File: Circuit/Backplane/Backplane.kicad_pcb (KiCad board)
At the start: 2 copper layers, 90.2 x 288.5 mm, 86 parts, among them CON1 Peripheral bridge, CON2 Power distributor, J1 USB_OTG, J2 power_source_mode, J3 general_power_source, J4 pneumatic, J5 pressure_sensor, J6 RS232_DVL, P1 imaging_sonar, P2 DVL, P3 computer1, P4 computer2, P5 ethernet_switch, P6 general, Q1 BC817-40, U1 LM1117-3.3, U2 TUSB4041I, U3 TLV73311PDBVT, Y1 24MHz

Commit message: re-commmit edit
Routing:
- net GND: track 74.5 -> 94.5 mm, vias 8 -> 14
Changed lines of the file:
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@@
     (thickness 1.6)
     (drawings 52)
-    (tracks 1115)
+    (tracks 1135)
     (zones 0)
     (modules 86)
@@
   )
   (setup
-    (last_trace_width 0.254)
+    (last_trace_width 0.381)
     (user_trace_width 0.381)
     (user_trace_width 0.508)
@@
     (user_trace_width 1.27)
     (trace_clearance 0.2032)
-    (zone_clearance 0.1524)
+    (zone_clearance 0.381)
     (zone_45_only no)
     (trace_min 0.2032)
@@
   (segment (start 155.966 254.332) (end 155.028 255.27) (width 0.254) (layer F.Cu) (net 2))
   (segment (start 155.966 253.432) (end 155.966 254.332) (width 0.254) (layer F.Cu) (net 2))
+  (segment (start 163.8 26.8) (end 163.8 25.969) (width 0.381) (layer F.Cu) (net 3))
+  (segment (start 163.8 25.969) (end 165.02379 24.74521) (width 0.381) (layer F.Cu) (net 3))
+  (segment (start 165.02379 24.74521) (end 165.02379 13.757744) (width 0.381) (layer F.Cu) (net 3))
+  (segment (start 165.02379 13.757744) (end 163.8632 12.597154) (width 0.381) (layer F.Cu) (net 3))
+  (segment (start 163.8632 12.597154) (end 163.8632 11.589313) (width 0.381) (layer F.Cu) (net 3))
   (segment (start 139.446 36.576) (end 140.72871 35.29329) (width 0.381) (layer F.Cu) (net 3))
   (segment (start 140.72871 35.29329) (end 155.19151 35.29329) (width 0.381) (layer F.Cu) (net 3))
   (segment (start 155.19151 35.29329) (end 163.7132 26.7716) (width 0.381) (layer F.Cu) (net 3))
   (segment (start 163.7132 26.7716) (end 163.8632 26.7716) (width 0.381) (layer F.Cu) (net 3))
-  (segment (start 164.85006 13.584014) (end 163.8632 12.597154) (width 0.381) (layer F.Cu) (net 3))
-  (segment (start 163.8632 12.597154) (end 163.8632 11.589313) (width 0.381) (layer F.Cu) (net 3))
   (segment (start 96.52 193.04) (end 86.36 203.2) (width 0.381) (layer F.Cu) (net 3))
   (segment (start 86.36 203.2) (end 86.36 251.46) (width 0.381) (layer F.Cu) (net 3))
@@
   (segment (start 139.446 36.576) (end 116.84 59.182) (width 0.381) (layer B.Cu) (net 3))
   (via (at 139.446 36.576) (size 1.10236) (drill 0.6096) (layers F.Cu B.Cu) (net 3))
-  (segment (start 164.85006 13.584014) (end 164.85006 24.91894) (width 0.381) (layer F.Cu) (net 3))
-  (segment (start 164.85006 24.91894) (end 163.8 25.969) (width 0.381) (layer F.Cu) (net 3))
-  (segment (start 163.8 25.969) (end 163.8 26.8) (width 0.381) (layer F.Cu) (net 3))
   (segment (start 144.044724 90.8682) (end 144.044724 91.8742) (width 0.381) (layer F.Cu) (net 3))
   (segment (start 151.738524 99.568) (end 152.869524 99.568) (width 0.381) (layer F.Cu) (net 3))
@@
   (segment (start 123.392 246.686) (end 125.984 249.278) (width 0.254) (layer F.Cu) (net 101))
   (segment (start 125.984 249.278) (end 125.984 249.428) (width 0.254) (layer F.Cu) (net 101))
+  (segment (start 98.48 237.998) (end 97.4344 237.998) (width 0.254) (layer F.Cu) (net 103))
+  (segment (start 97.4344 237.998) (end 96.3168 239.1156) (width 0.254) (layer F.Cu) (net 103))
+  (via (at 96.3168 239.1156) (size 1.10236) (drill 0.6096) (layers F.Cu B.Cu) (net 103))
+  (segment (start 98.48 235.42) (end 95.3388 235.42) (width 0.254) (layer F.Cu) (net 103))
+  (segment (start 95.3388 235.42) (end 95.3008 235.458) (width 0.254) (layer F.Cu) (net 103))
+  (via (at 95.3008 235.458) (size 1.10236) (drill 0.6096) (layers F.Cu B.Cu) (net 103))
+  (segment (start 139.868 241.3) (end 139.868 243.7736) (width 0.254) (layer F.Cu) (net 103))
+  (via (at 139.7 243.9416) (size 1.10236) (drill 0.6096) (layers F.Cu B.Cu) (net 103))
+  (segment (start 139.868 243.7736) (end 139.7 243.9416) (width 0.254) (layer F.Cu) (net 103))
+  (segment (start 139.446 239.268) (end 139.446 240.878) (width 0.254) (layer F.Cu) (net 103))
+  (segment (start 139.446 240.878) (end 139.868 241.3) (width 0.254) (layer F.Cu) (net 103))
+  (segment (start 139.7 237.236) (end 143.5608 237.236) (width 0.254) (layer F.Cu) (net 103))
+  (segment (start 143.5608 237.236) (end 144.1704 236.6264) (width 0.254) (layer F.Cu) (net 103))
+  (via (at 144.1704 236.6264) (size 1.10236) (drill 0.6096) (layers F.Cu B.Cu) (net 103))
+  (segment (start 141.392 228.6) (end 143.0528 228.6) (width 0.254) (layer F.Cu) (net 103))
+  (segment (start 143.0528 228.6) (end 143.51 229.0572) (width 0.254) (layer F.Cu) (net 103))
+  (via (at 143.51 229.0572) (size 1.10236) (drill 0.6096) (layers F.Cu B.Cu) (net 103))
+  (segment (start 141.404 224.282) (end 143.3576 224.282) (width 0.254) (layer F.Cu) (net 103))
+  (segment (start 143.3576 224.282) (end 143.5608 224.4852) (width 0.254) (layer F.Cu) (net 103))
+  (via (at 143.5608 224.4852) (size 1.10236) (drill 0.6096) (layers F.Cu B.Cu) (net 103))
   (segment (start 83.058 108.204) (end 83.058 103.886) (width 0.254) (layer F.Cu) (net 103))
   (via (at 83.058 103.886) (size 1.10236) (drill 0.6096) (layers F.Cu B.Cu) (net 103))
@@
   (segment (start 147.97568 26.7716) (end 147.869 26.66492) (width 0.381) (layer F.Cu) (net 145))
   (zone (net 103) (net_name GND) (layer F.Cu) (hatch edge 0.508)
-    (connect_pads yes (clearance 0.1524))
+    (connect_pads yes (clearance 0.381))
     (min_thickness 0.254)
     (fill yes (arc_segments 16) (thermal_gap 0.508) (thermal_bridge_width 0.508))
@@
   )
   (zone (net 103) (net_name GND) (layer B.Cu) (hatch edge 0.508)
-    (connect_pads yes (clearance 0.1524))
+    (connect_pads yes (clearance 0.381))
     (min_thickness 0.254)
     (fill yes (arc_segments 16) (thermal_gap 0.508) (thermal_bridge_width 0.508))

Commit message: fix leds position on pcb
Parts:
- moved R15 22.5 mm to (147.3, 0.00), turned to 0 degrees
- moved D2 22.2 mm to (162.6, 0.00)
- moved R17 18.1 mm to (147.3, 22.9), turned to 0 degrees
- moved D4 18.1 mm to (162.6, 22.9)
- moved D5 14.6 mm to (162.6, 3.81)
- moved R18 14.6 mm to (147.3, 3.81), turned to 0 degrees
- moved R16 11.3 mm to (147.3, 11.4), turned to 0 degrees
- moved D3 10.2 mm to (162.6, 11.4)
- moved R2 7.48 mm to (147.3, 19.1), turned to 0 degrees
- moved D1 7.46 mm to (162.6, 19.1)
- moved R20 0.72 mm to (147.3, 7.62), turned to 0 degrees
- moved R19 0.60 mm to (147.3, 15.2), turned to 0 degrees
- moved R21 0.55 mm to (147.3, 26.7)
- moved D7 0.46 mm to (162.6, 7.62)
- moved D6 0.25 mm to (162.6, 15.2)
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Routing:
- net GND: track 94.5 -> 56.3 mm, vias 14 -> 13
- net +BATT: track 190.9 -> 211.1 mm
- net +3V3: track 313.6 -> 294.3 mm
- net VBUS: track 286.4 -> 270.4 mm
- net +12V: track 344.6 -> 357.8 mm
- net GNDA: track 186.6 -> 198.9 mm
- net +5V: track 513.6 -> 506.3 mm
- net Net-(D2-Pad1): track 19.7 -> 13.0 mm
- net Net-(D3-Pad1): track 18.6 -> 13.0 mm
- net Net-(D5-Pad1): track 18.5 -> 13.0 mm
- net Net-(D6-Pad1): track 18.2 -> 13.0 mm
- net Net-(D7-Pad1): track 17.9 -> 13.0 mm
- net Net-(D4-Pad1): track 17.6 -> 13.0 mm
- net Net-(D1-Pad1): track 17.2 -> 13.0 mm
- net Net-(D8-Pad1): track 13.8 -> 13.0 mm

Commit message: add gerberfile for production
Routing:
- net (no net): track 0.00 -> 0.05 mm, vias 0 -> 2
- net GND: vias 13 -> 11
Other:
- board text added: "ZEABUS 2018 Backplane Rev 1.0"
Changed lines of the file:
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@@
   (general
     (links 258)
-    (no_connects 0)
-    (area 76.124999 -26.745001 166.445001 261.949001)
+    (no_connects 2)
+    (area 54.634001 -26.745001 180.57 277.020001)
     (thickness 1.6)
-    (drawings 52)
+    (drawings 54)
     (tracks 1078)
     (zones 0)
@@
   )
   (setup
-    (last_trace_width 0.381)
+    (last_trace_width 0.254)
     (user_trace_width 0.381)
     (user_trace_width 0.508)
@@
     (visible_elements 7FFFFFFF)
     (pcbplotparams
-      (layerselection 0x00030_80000001)
-      (usegerberextensions false)
+      (layerselection 0x0103c_80000001)
+      (usegerberextensions true)
       (excludeedgelayer true)
       (linewidth 0.100000)
@@
       (plotinvisibletext false)
       (padsonsilk false)
-      (subtractmaskfromsilk false)
+      (subtractmaskfromsilk true)
       (outputformat 1)
       (mirror false)
-      (drillshape 1)
+      (drillshape 0)
       (scaleselection 1)
-      (outputdirectory ""))
+      (outputdirectory plot/))
   )
   (net 0 "")
@@
     )
   )
+  (dimension 288.544 (width 0.3) (layer Margin)
+    (gr_text "288.544 mm" (at 184.8396 117.602 90) (layer Margin)
+      (effects (font (size 1.5 1.5) (thickness 0.3)))
+    )
+    (feature1 (pts (xy 166.37 -26.67) (xy 186.1896 -26.67)))
+    (feature2 (pts (xy 166.37 261.874) (xy 186.1896 261.874)))
+    (crossbar (pts (xy 183.4896 261.874) (xy 183.4896 -26.67)))
+    (arrow1a (pts (xy 183.4896 -26.67) (xy 184.076021 -25.543496)))
+    (arrow1b (pts (xy 183.4896 -26.67) (xy 182.903179 -25.543496)))
+    (arrow2a (pts (xy 183.4896 261.874) (xy 184.076021 260.747496)))
+    (arrow2b (pts (xy 183.4896 261.874) (xy 182.903179 260.747496)))
+  )
+  (gr_text "ZEABUS 2018\nBackplane Rev 1.0" (at 122.5804 -18.5928) (layer F.SilkS)
+    (effects (font (size 1.5 1.5) (thickness 0.3)))
+  )
   (dimension 4.9784 (width 0.3) (layer Margin)
     (gr_text "4.978 mm" (at 163.83 204.3392) (layer Margin)
@@
     (arrow2b (pts (xy 91.44 119.634) (xy 90.853579 118.507496)))
   )
+  (via (at 95.3008 235.458) (size 1.10236) (drill 0.6096) (layers F.Cu B.Cu) (net 0))
+  (segment (start 95.3388 235.42) (end 95.3008 235.458) (width 0.254) (layer F.Cu) (net 0))
+  (via (at 144.1704 236.6264) (size 1.10236) (drill 0.6096) (layers F.Cu B.Cu) (net 0))
   (segment (start 163.6522 17.1196) (end 163.6522 15.2478) (width 0.381) (layer F.Cu) (net 1))
   (segment (start 163.6522 15.2478) (end 163.66 15.24) (width 0.381) (layer F.Cu) (net 1))
@@
   (via (at 143.51 7.5946) (size 1.10236) (drill 0.6096) (layers F.Cu B.Cu) (net 103))
   (segment (start 146.22 7.62) (end 146.07 7.62) (width 0.381) (layer F.Cu) (net 103))
-  (via (at 95.3008 235.458) (size 1.10236) (drill 0.6096) (layers F.Cu B.Cu) (net 103))
   (segment (start 98.48 237.998) (end 97.4344 237.998) (width 0.254) (layer F.Cu) (net 103))
   (segment (start 97.4344 237.998) (end 96.3168 239.1156) (width 0.254) (layer F.Cu) (net 103))
   (via (at 96.3168 239.1156) (size 1.10236) (drill 0.6096) (layers F.Cu B.Cu) (net 103))
-  (segment (start 95.3388 235.42) (end 95.3008 235.458) (width 0.254) (layer F.Cu) (net 103))
   (segment (start 139.868 241.3) (end 139.868 243.7736) (width 0.254) (layer F.Cu) (net 103))
   (via (at 139.7 243.9416) (size 1.10236) (drill 0.6096) (layers F.Cu B.Cu) (net 103))
@@
   (segment (start 139.446 239.268) (end 139.446 240.878) (width 0.254) (layer F.Cu) (net 103))
   (segment (start 139.446 240.878) (end 139.868 241.3) (width 0.254) (layer F.Cu) (net 103))
-  (via (at 144.1704 236.6264) (size 1.10236) (drill 0.6096) (layers F.Cu B.Cu) (net 103))
   (segment (start 141.392 228.6) (end 143.0528 228.6) (width 0.254) (layer F.Cu) (net 103))
   (segment (start 143.0528 228.6) (end 143.51 229.0572) (width 0.254) (layer F.Cu) (net 103))

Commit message: edited footprint
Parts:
- U2: footprint Housings_QFP:HTQFP-64-1EP_10x10mm_Pitch0.5mm_ThermalPad -> Zeabus:HTQFP-64-1EP_10x10mm_Pitch0.5mm_ThermalPad

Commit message: Rotate Power_dist board on BackPlane
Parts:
- moved C25 75.6 mm to (83.2, 32.6), turned to 0 degrees
- moved L2 74.1 mm to (83.2, 36.6), turned to 180 degrees
- moved CON2 66.2 mm to (91.4, 39.2), turned to 270 degrees
- moved R22 0.52 mm to (147.3, 32.9)
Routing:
- net +1V1: track 269.8 -> 333.1 mm, vias 4 -> 2
- net Net-(CON2-PadB15): track 168.0 -> 221.2 mm
- net Net-(CON2-PadB14): track 168.7 -> 221.2 mm
- net GNDA: track 198.9 -> 147.2 mm, vias 5 -> 1
- net genPow: track 154.8 -> 109.7 mm, vias 0 -> 2
- net +12V: track 357.8 -> 398.5 mm, vias 3 -> 2
- net VBUS: track 270.4 -> 305.5 mm
- net GND: track 56.3 -> 85.2 mm, vias 11 -> 17
- net VPCIE: track 231.4 -> 206.2 mm, vias 6 -> 0
- net +BATT: track 211.1 -> 190.5 mm, vias 5 -> 2
- net Net-(CON1-PadA4): track 157.7 -> 138.8 mm, vias 3 -> 1
- net Net-(C26-Pad1): track 33.4 -> 22.4 mm
- net Net-(CON1-PadA6): track 146.3 -> 137.7 mm, vias 3 -> 1
- net +3V3: track 294.3 -> 289.1 mm
- net Net-(CON1-PadA12): track 93.0 -> 97.6 mm
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
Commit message: adjusted traces width, traces lining on Backplane
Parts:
- moved C23 5.87 mm to (124.7, 194.1)
- moved L1 5.83 mm to (124.7, 191.1)
- moved C26 3.62 mm to (149.2, 96.5)
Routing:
- net +5V: track 510.4 -> 497.2 mm
- net Net-(C14-Pad1): track 198.1 -> 186.6 mm
- net Net-(C23-Pad1): track 24.1 -> 16.8 mm
- net +3V3: track 289.1 -> 294.2 mm, vias 4 -> 5
- net GND: track 85.2 -> 82.0 mm, vias 17 -> 18
- net (no net): track 2.62 -> 0.00 mm, vias 2 -> 0
- net +1V1: track 333.1 -> 335.1 mm
- net +12V: track 398.5 -> 399.6 mm
- net VPCIE: track 206.2 -> 205.3 mm
- net Net-(C26-Pad1): track 22.4 -> 21.9 mm
- net VBUS: track 305.5 -> 305.4 mm, vias 2 -> 3

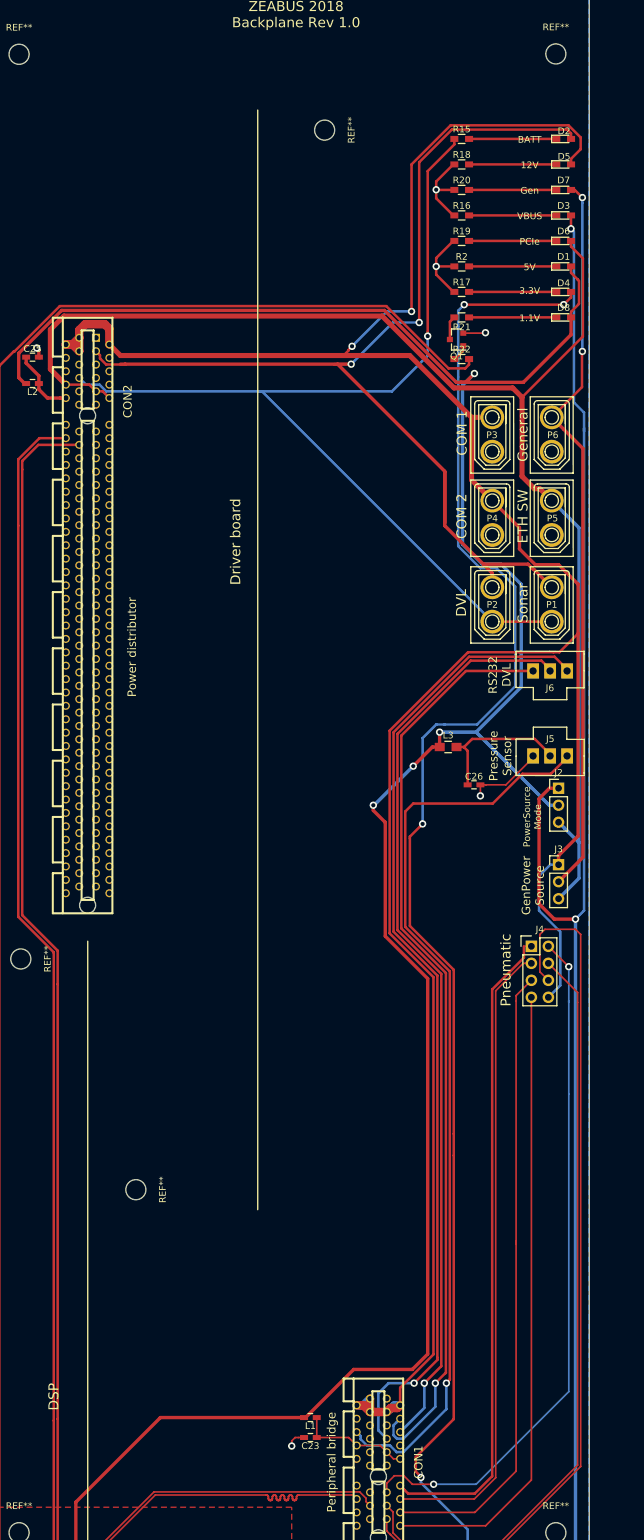
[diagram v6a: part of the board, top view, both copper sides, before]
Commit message: added power mode socket silkskins description and NO. and Note silkskin on Backplane
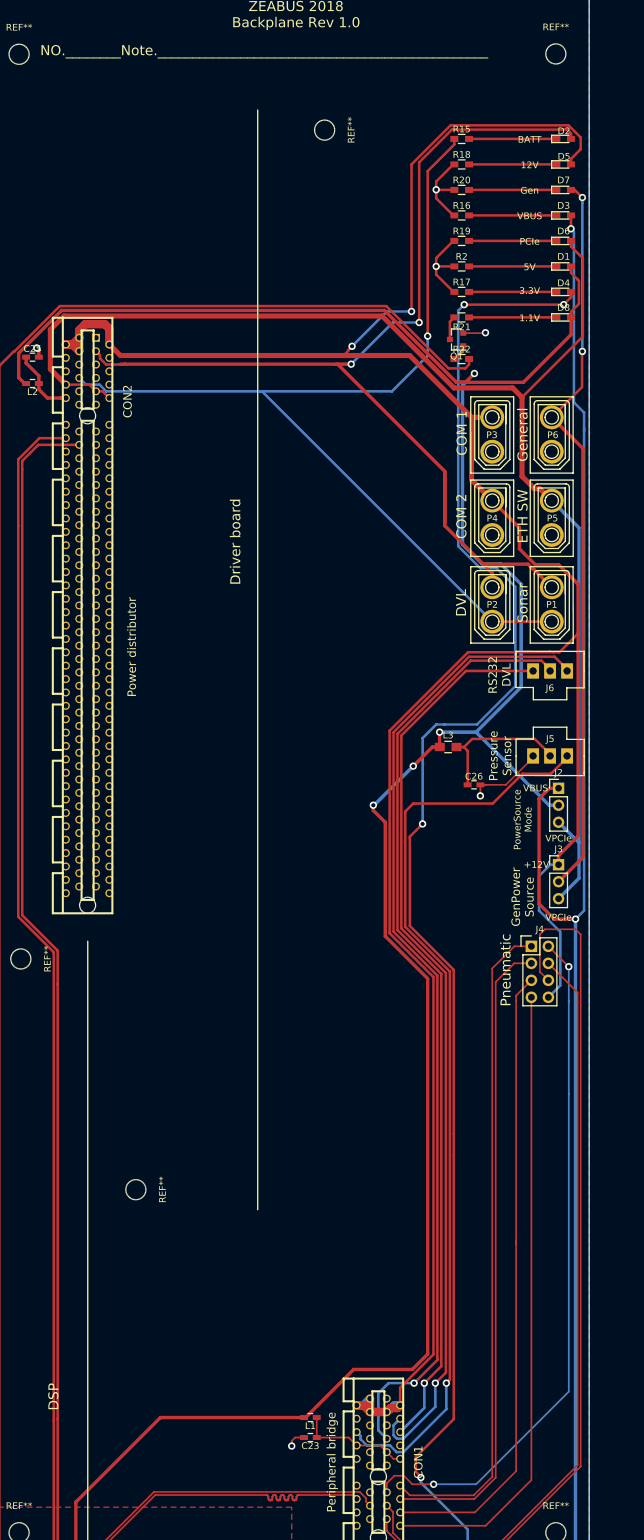
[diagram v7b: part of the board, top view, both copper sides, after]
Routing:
- net Net-(CON1-PadA12): track 97.6 -> 98.7 mm
- net Net-(CON1-PadA14): track 95.4 -> 96.2 mm
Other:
- board text added: "+12V"
- board text added: "NO.________Note.________________________________________________"
- board text added: "VPCIe"
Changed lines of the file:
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@@
     (links 258)
     (no_connects 0)
-    (area 54.634001 -26.745001 192.053886 277.020001)
+    (area 76.124999 -26.745001 166.445001 261.949001)
     (thickness 1.6)
-    (drawings 54)
-    (tracks 1043)
+    (drawings 59)
+    (tracks 1041)
     (zones 0)
     (modules 86)
@@
     )
   )
+  (gr_text NO.________Note.________________________________________________ (at 84.328 -13.208) (layer F.SilkS)
+    (effects (font (size 1.5 1.5) (thickness 0.3)) (justify left))
+  )
+  (gr_text VPCIe (at 161.798 116.332) (layer F.SilkS)
+    (effects (font (size 1 1) (thickness 0.25)))
+  )
+  (gr_text +12V (at 158.496 108.458) (layer F.SilkS)
+    (effects (font (size 1 1) (thickness 0.25)))
+  )
+  (gr_text VPCIe (at 161.798 104.521) (layer F.SilkS)
+    (effects (font (size 1 1) (thickness 0.25)))
+  )
+  (gr_text VBUS (at 158.369 97.028) (layer F.SilkS)
+    (effects (font (size 1 1) (thickness 0.25)))
+  )
   (gr_text Sonar (at 156.464 69.342 90) (layer F.SilkS)
     (effects (font (size 1.5 1.5) (thickness 0.3)))
@@
     (effects (font (size 1.27 1.27) (thickness 0.3)))
   )
-  (gr_text "PowerSource\nMode" (at 157.8864 101.2952 90) (layer F.SilkS)
+  (gr_text "PowerSource\nMode" (at 156.464 101.727 90) (layer F.SilkS)
     (effects (font (size 1.016 1.016) (thickness 0.254)))
   )
-  (gr_text "GenPower\nSource" (at 157.988 111.5568 90) (layer F.SilkS)
+  (gr_text "GenPower\nSource" (at 156.464 113.284 90) (layer F.SilkS)
     (effects (font (size 1.27 1.27) (thickness 0.3)))
   )
@@
   (segment (start 146.419724 90.8682) (end 146.544724 90.8682) (width 0.381) (layer F.Cu) (net 12))
   (segment (start 146.402273 91.010651) (end 146.544724 90.8682) (width 0.254) (layer F.Cu) (net 12))
-  (segment (start 149.276006 202.438) (end 139.32154 202.438) (width 0.381) (layer F.Cu) (net 13))
-  (segment (start 139.32154 202.438) (end 138.724639 201.841099) (width 0.381) (layer F.Cu) (net 13))
-  (segment (start 138.724639 201.841099) (end 138.1252 201.24166) (width 0.381) (layer F.Cu) (net 13))
-  (segment (start 151.87929 199.834716) (end 149.276006 202.438) (width 0.381) (layer F.Cu) (net 13))
-  (segment (start 151.87929 127.087001) (end 151.87929 199.834716) (width 0.381) (layer F.Cu) (net 13))
-  (segment (start 156.6164 120.65) (end 156.6164 122.349892) (width 0.381) (layer F.Cu) (net 13))
-  (segment (start 156.6164 122.349892) (end 151.87929 127.087001) (width 0.381) (layer F.Cu) (net 13))
-  (segment (start 156.6164 120.65) (end 157.734 120.65) (width 0.254) (layer F.Cu) (net 13))
+  (segment (start 138.1252 201.24166) (end 139.57554 202.692) (width 0.254) (layer F.Cu) (net 13))
+  (segment (start 139.57554 202.692) (end 149.111808 202.692) (width 0.254) (layer F.Cu) (net 13))
+  (segment (start 151.87929 199.924518) (end 151.87929 123.96471) (width 0.254) (layer F.Cu) (net 13))
+  (segment (start 149.111808 202.692) (end 151.87929 199.924518) (width 0.254) (layer F.Cu) (net 13))
+  (segment (start 151.87929 123.96471) (end 155.194 120.65) (width 0.254) (layer F.Cu) (net 13))
+  (segment (start 155.194 120.65) (end 157.734 120.65) (width 0.254) (layer F.Cu) (net 13))
   (segment (start 143.129 201.041) (end 149.479 201.041) (width 0.254) (layer B.Cu) (net 14))
   (segment (start 149.479 201.041) (end 163.322 187.198) (width 0.254) (layer B.Cu) (net 14))
@@
   (segment (start 160.274 120.65) (end 163.322 123.698) (width 0.254) (layer F.Cu) (net 14))
   (via (at 163.322 123.698) (size 1.10236) (drill 0.6096) (layers F.Cu B.Cu) (net 14))
-  (segment (start 157.734 123.19) (end 156.512686 123.19) (width 0.254) (layer F.Cu) (net 15))
-  (segment (start 152.4 127.302686) (end 152.4 200.0504) (width 0.254) (layer F.Cu) (net 15))
-  (segment (start 156.512686 123.19) (end 152.4 127.302686) (width 0.254) (layer F.Cu) (net 15))
-  (segment (start 152.4 200.0504) (end 149.20976 203.24064) (width 0.254) (layer F.Cu) (net 15))
-  (segment (start 149.20976 203.24064) (end 138.1252 203.24064) (width 0.254) (layer F.Cu) (net 15))
+  (segment (start 138.1252 203.24064) (end 149.20976 203.24064) (width 0.254) (layer F.Cu) (net 15))
+  (segment (start 155.194 123.19) (end 157.734 123.19) (width 0.254) (layer F.Cu) (net 15))
+  (segment (start 149.20976 203.24064) (end 152.4 200.0504) (width 0.254) (layer F.Cu) (net 15))
+  (segment (start 152.4 200.0504) (end 152.4 125.984) (width 0.254) (layer F.Cu) (net 15))
+  (segment (start 152.4 125.984) (end 155.194 123.19) (width 0.254) (layer F.Cu) (net 15))
   (segment (start 164.64279 198.184618) (end 164.64279 129.032) (width 0.254) (layer F.Cu) (net 16))
   (segment (start 164.64279 129.032) (end 164.64279 127.55879) (width 0.254) (layer F.Cu) (net 16))

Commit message: moved Power_distributor PCIe higher and adjusted NO. and Note silkskin
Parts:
- moved CON2 52.1 mm to (91.4, -12.9)
- moved C25 39.7 mm to (81.9, -7.11), turned to 180 degrees
- moved L2 39.4 mm to (81.9, -2.84)
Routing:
- net +1V1: track 335.1 -> 416.4 mm, vias 2 -> 4
- net +12V: track 399.6 -> 469.8 mm
- net +5V: track 497.2 -> 543.6 mm
- net Net-(CON2-PadB15): track 221.2 -> 251.0 mm
- net Net-(CON2-PadB14): track 221.2 -> 250.1 mm
- net GNDA: track 147.2 -> 168.3 mm, vias 1 -> 3
- net VPCIE: track 205.3 -> 214.0 mm, vias 0 -> 2
- net +BATT: track 190.5 -> 198.7 mm, vias 2 -> 3
- net Net-(C25-Pad1): track 10.2 -> 12.7 mm
- net GND: track 82.0 -> 82.6 mm
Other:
- board text added: "NO.________ Note________________________________________"
- board text removed: "NO.________Note.________________________________________________"
